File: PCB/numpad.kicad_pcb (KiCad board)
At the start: 2 copper layers, 106.4 x 115.1 mm, 91 parts, among them J1 AVR-ISP-6, J2 Conn_01x04_Female, SW1 SW_Push, U1 ProMicro

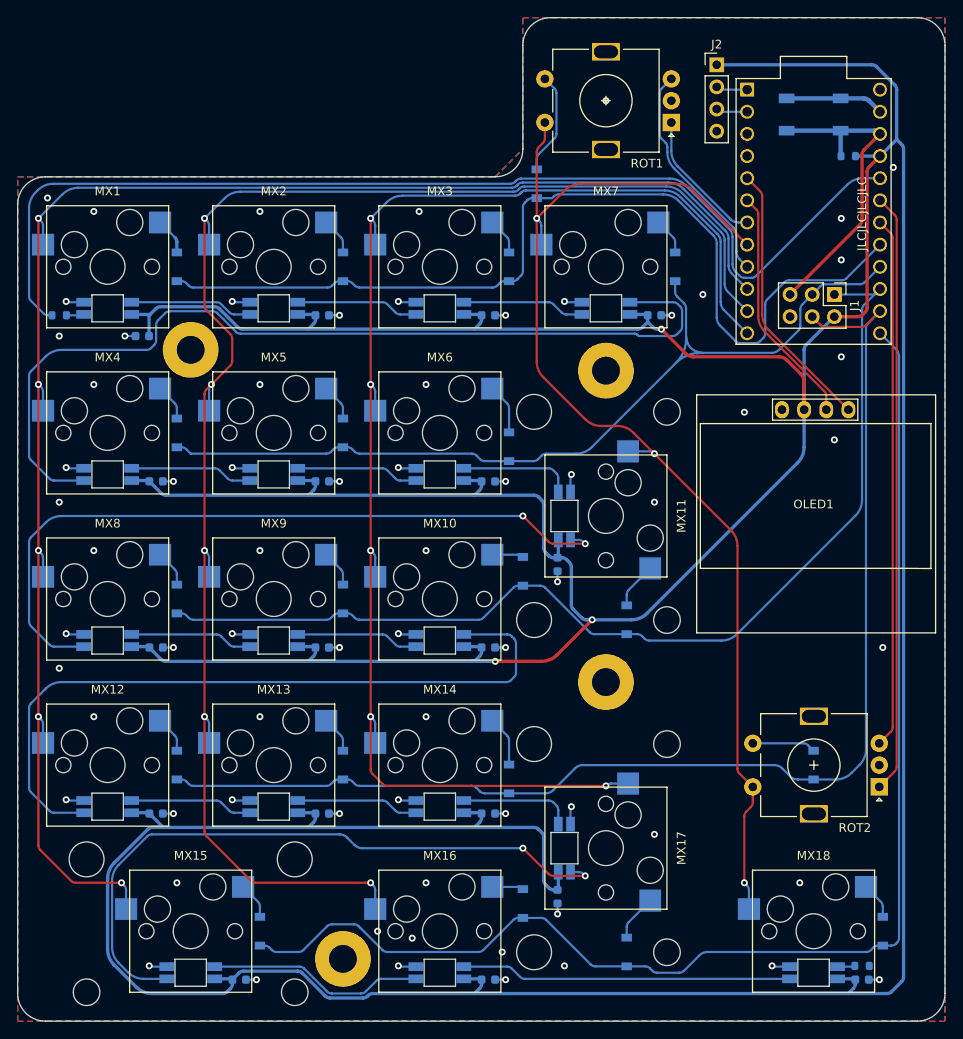
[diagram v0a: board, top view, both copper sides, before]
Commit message: Added 3d models, cleaned up traces, exported gerbers
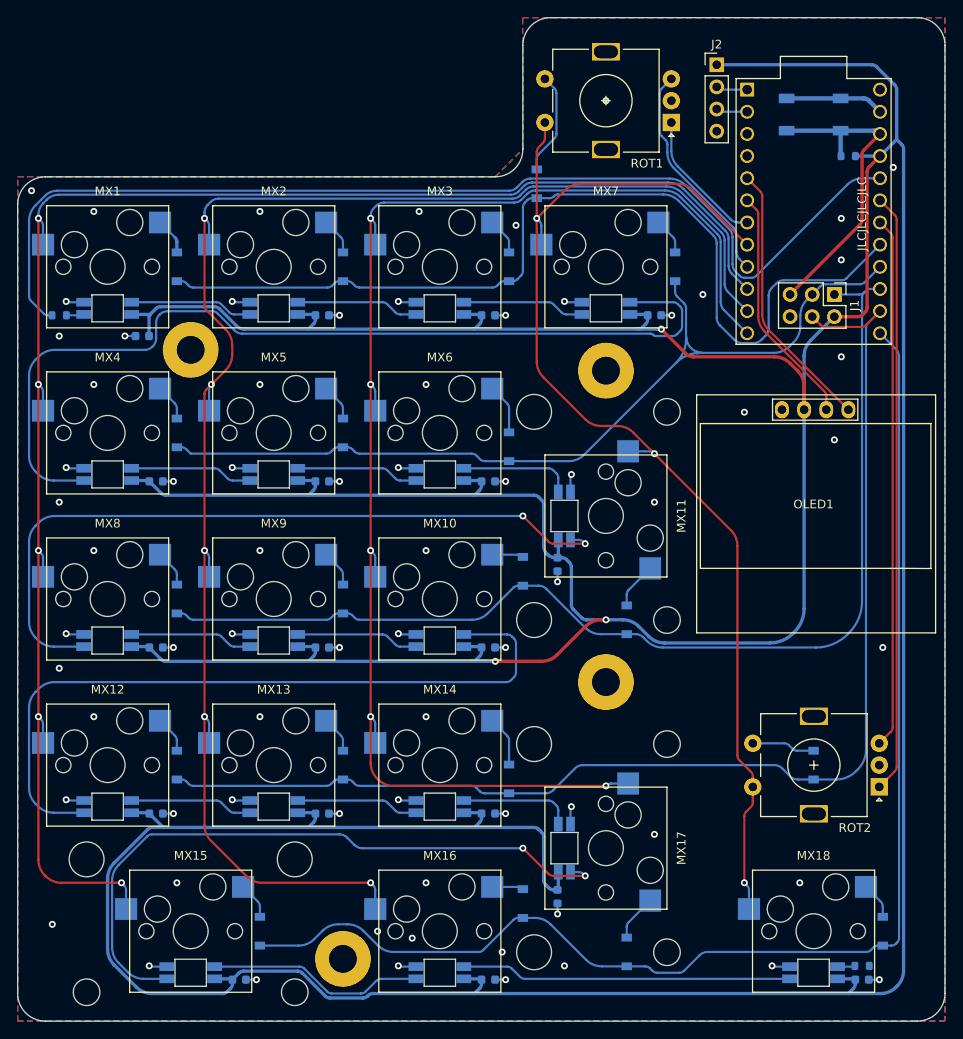
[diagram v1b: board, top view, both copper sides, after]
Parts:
- H1, H2, H3, H4: value Hole -> M3
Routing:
- net +5V: track 626.1 -> 641.3 mm
- net MISO: track 120.0 -> 127.2 mm
- net COL0: track 189.4 -> 191.2 mm
- net ROW4: track 151.8 -> 150.8 mm
- net BKL_DATA_IN: track 124.5 -> 123.6 mm
- net Net-(LED4-Pad2): track 105.8 -> 106.7 mm
- net Net-(LED11-Pad2): track 84.2 -> 84.9 mm
- net Net-(LED8-Pad2): track 84.8 -> 85.5 mm
- net GND: vias 70 -> 72
